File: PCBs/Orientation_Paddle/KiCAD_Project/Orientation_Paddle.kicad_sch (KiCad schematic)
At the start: 54 parts, among them J1 NP_Conn_01x04_Relief, J2 1-0001205, J3 NP_Conn_01x03_Relief, J4 NP_Conn_01x02_Relief, J5 NP_Conn_01x02_Relief, J6 NP_Conn_01x04, J7 NP_Conn_01x04, J8 NP_Conn_01x02, U1 1-0001232, U2 1-0001471, U3 1-0000207, Y1 1-0000721

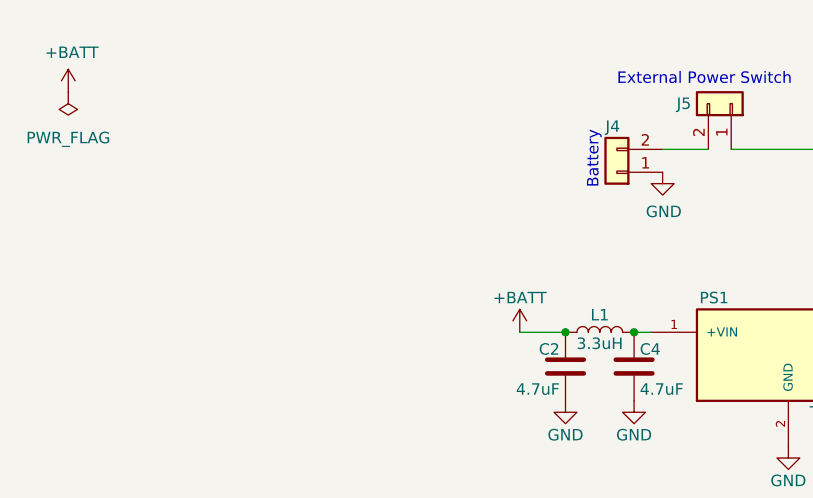
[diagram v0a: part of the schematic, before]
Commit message: Orientation Paddle Revisions: Board resize to nice numbers Fixed Footprint/Symbols causing ERC Errors Fixed remaining ERC Errors (Schematic and PCB)
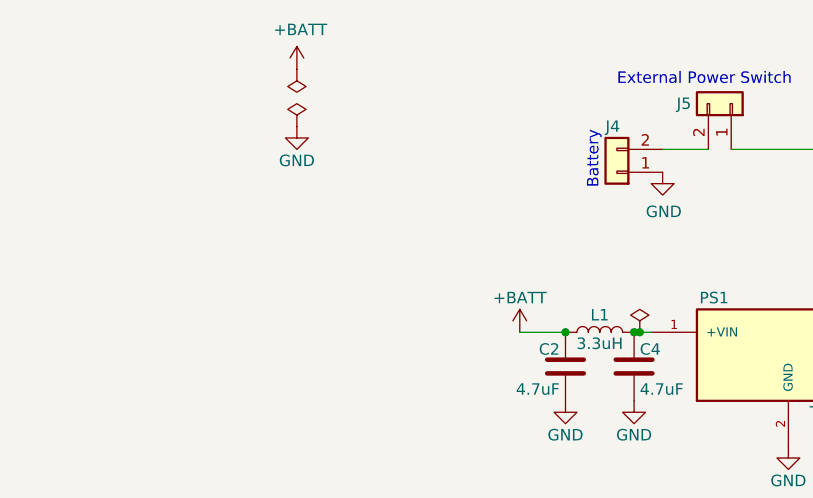
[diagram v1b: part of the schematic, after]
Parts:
- JP1, JP2, JP5, JP6: now left out of the parts list
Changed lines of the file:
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@@
 	)
 	(junction
+		(at 43.18 46.99)
+		(diameter 0)
+		(color 0 0 0 0)
+	)
+	(junction
 		(at 250.825 101.6)
 		(diameter 0)
@@
 	(wire
 		(pts
+			(xy 43.18 46.99) (xy 44.45 46.99)
+		)
+		(stroke
+			(width 0)
+			(type default)
+		)
+	)
+	(wire
+		(pts
 			(xy 255.905 104.14) (xy 255.905 104.775)
 		)
@@
 	(wire
 		(pts
-			(xy 42.545 46.99) (xy 44.45 46.99)
+			(xy 42.545 46.99) (xy 43.18 46.99)
 		)
 		(stroke
@@
 		(at 208.28 124.46 270)
 		(unit 1)
-		(exclude_from_sim no)
-		(in_bom yes)
+		(exclude_from_sim yes)
+		(in_bom no)
 		(on_board yes)
 		(dnp no)
@@
 	(symbol
 		(lib_id "power:PWR_FLAG")
-		(at -20.32 20.32 180)
+		(at 5.08 17.78 180)
 		(unit 1)
 		(exclude_from_sim no)
@@
 		(fields_autoplaced yes)
 		(property "Reference" "#FLG03"
-			(at -20.32 22.225 0)
+			(at 5.08 19.685 0)
 			(effects
 				(font
@@
 		)
 		(property "Value" "PWR_FLAG"
-			(at -20.32 25.4 0)
+			(at 5.08 22.86 0)
 			(effects
 				(font
 					(size 1.27 1.27)
 				)
+				(hide yes)
 			)
 		)
 		(property "Footprint" ""
-			(at -20.32 20.32 0)
+			(at 5.08 17.78 0)
 			(effects
 				(font
@@
 		)
 		(property "Datasheet" "~"
-			(at -20.32 20.32 0)
+			(at 5.08 17.78 0)
 			(effects
 				(font
@@
 		)
 		(property "Description" "Special symbol for telling ERC where power comes from"
-			(at -20.32 20.32 0)
+			(at 5.08 17.78 0)
 			(effects
 				(font
@@
 	)
 	(symbol
+		(lib_id "power:GND")
+		(at 5.08 24.13 0)
+		(unit 1)
+		(exclude_from_sim no)
+		(in_bom yes)
+		(on_board yes)
+		(dnp no)
+		(property "Reference" "#PWR056"
+			(at 5.08 30.48 0)
+			(effects
+				(font
+					(size 1.27 1.27)
+				)
+				(hide yes)
+			)
+		)
+		(property "Value" "GND"
+			(at 5.08 27.94 0)
+			(effects
+				(font
+					(size 1.27 1.27)
+				)
+			)
+		)
+		(property "Footprint" ""
+			(at 5.08 24.13 0)
+			(effects
+				(font
+					(size 1.27 1.27)
+				)
+				(hide yes)
+			)
+		)
+		(property "Datasheet" ""
+			(at 5.08 24.13 0)
+			(effects
+				(font
+					(size 1.27 1.27)
+				)
+				(hide yes)
+			)
+		)
+		(property "Description" "Power symbol creates a global label with name \"GND\" , ground"
+			(at 5.08 24.13 0)
+			(effects
+				(font
+					(size 1.27 1.27)
+				)
+				(hide yes)
+			)
+		)
+		(pin "1"
+		)
+		(instances
+			(project "Orientation_Paddle"
+				(path "/6c14ab86-27f6-4df4-bc2f-a5f06a463ed0"
+					(reference "#PWR056")
+					(unit 1)
+				)
+			)
+		)
+	)
+	(symbol
 		(lib_id "np_connectors:NP_Conn_01x03_Relief")
 		(at 20.32 157.48 180)
@@
 	)
 	(symbol
+		(lib_id "power:PWR_FLAG")
+		(at 5.08 24.13 0)
+		(unit 1)
+		(exclude_from_sim no)
+		(in_bom yes)
+		(on_board yes)
+		(dnp no)
+		(fields_autoplaced yes)
+		(property "Reference" "#FLG04"
+			(at 5.08 22.225 0)
+			(effects
+				(font
+					(size 1.27 1.27)
+				)
+				(hide yes)
+			)
+		)
+		(property "Value" "PWR_FLAG"
+			(at 5.08 19.05 0)
+			(effects
+				(font
+					(size 1.27 1.27)
+				)
+				(hide yes)
+			)
+		)
+		(property "Footprint" ""
+			(at 5.08 24.13 0)
+			(effects
+				(font
+					(size 1.27 1.27)
+				)
+				(hide yes)
+			)
+		)
+		(property "Datasheet" "~"
+			(at 5.08 24.13 0)
+			(effects
+				(font
+					(size 1.27 1.27)
+				)
+				(hide yes)
+			)
+		)
+		(property "Description" "Special symbol for telling ERC where power comes from"
+			(at 5.08 24.13 0)
+			(effects
+				(font
+					(size 1.27 1.27)
+				)
+				(hide yes)
+			)
+		)
+		(pin "1"
+		)
+		(instances
+			(project "Orientation_Paddle"
+				(path "/6c14ab86-27f6-4df4-bc2f-a5f06a463ed0"
+					(reference "#FLG04")
+					(unit 1)
+				)
+			)
+		)
+	)
+	(symbol
 		(lib_id "capacitors_0603:1-0000007")
 		(at 245.11 74.93 0)
@@
 	(symbol
 		(lib_id "power:+BATT")
-		(at -20.32 20.32 0)
+		(at 5.08 17.78 0)
 		(unit 1)
 		(exclude_from_sim no)
@@
 		(dnp no)
 		(property "Reference" "#PWR055"
-			(at -20.32 24.13 0)
+			(at 5.08 21.59 0)
 			(effects
 				(font
@@
 		)
 		(property "Value" "+BATT"
-			(at -19.939 15.9258 0)
+			(at 5.461 13.3858 0)
 			(effects
 				(font
@@
 		)
 		(property "Footprint" ""
-			(at -20.32 20.32 0)
+			(at 5.08 17.78 0)
 			(effects
 				(font
@@
 		)
 		(property "Datasheet" ""
-			(at -20.32 20.32 0)
+			(at 5.08 17.78 0)
 			(effects
 				(font
@@
 		)
 		(property "Description" "Power symbol creates a global label with name \"+BATT\""
-			(at -20.32 20.32 0)
+			(at 5.08 17.78 0)
 			(effects
 				(font
@@
 		(mirror x)
 		(unit 1)
-		(exclude_from_sim no)
-		(in_bom yes)
+		(exclude_from_sim yes)
+		(in_bom no)
 		(on_board yes)
 		(dnp no)
@@
 			)
 		)
-		(property "Description" ""
+		(property "Description" "Linear Regulator Replacement DC DC Converter 1 Output 3.3V - - - 500mA 4.75V - 32V Input"
 			(at 59.69 49.53 0)
 			(effects
@@
 		(at 208.28 111.76 270)
 		(unit 1)
-		(exclude_from_sim no)
-		(in_bom yes)
+		(exclude_from_sim yes)
+		(in_bom no)
 		(on_board yes)
 		(dnp no)
@@
 	)
 	(symbol
+		(lib_id "power:PWR_FLAG")
+		(at 43.18 46.99 0)
+		(unit 1)
+		(exclude_from_sim no)
+		(in_bom yes)
+		(on_board yes)
+		(dnp no)
+		(fields_autoplaced yes)
+		(property "Reference" "#FLG02"
+			(at 43.18 45.085 0)
+			(effects
+				(font
+					(size 1.27 1.27)
+				)
+				(hide yes)
+			)
+		)
+		(property "Value" "PWR_FLAG"
+			(at 43.18 42.7365 0)
+			(effects
+				(font
+					(size 1.27 1.27)
+				)
+				(hide yes)
+			)
+		)
+		(property "Footprint" ""
+			(at 43.18 46.99 0)
+			(effects
+				(font
+					(size 1.27 1.27)
+				)
+				(hide yes)
+			)
+		)
+		(property "Datasheet" "~"
+			(at 43.18 46.99 0)
+			(effects
+				(font
+					(size 1.27 1.27)
+				)
+				(hide yes)
+			)
+		)
+		(property "Description" "Special symbol for telling ERC where power comes from"
+			(at 43.18 46.99 0)
+			(effects
+				(font
+					(size 1.27 1.27)
+				)
+				(hide yes)
+			)
+		)
+		(pin "1"
+		)
+		(instances
+			(project "Orientation_Paddle"
+				(path "/6c14ab86-27f6-4df4-bc2f-a5f06a463ed0"
+					(reference "#FLG02")
+					(unit 1)
+				)
+			)
+		)
+	)
+	(symbol
 		(lib_id "capacitors_0603:1-0000007")
 		(at 29.21 152.4 90)
@@
 		(mirror x)
 		(unit 1)
-		(exclude_from_sim no)
-		(in_bom yes)
+		(exclude_from_sim yes)
+		(in_bom no)
 		(on_board yes)
 		(dnp no)

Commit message: Fixed Orientation Paddle ERC Issues and Copper to Edge Clearence
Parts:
- H1, H2, H3, H4: now left out of the parts list
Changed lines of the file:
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@@
 		(unit 1)
 		(exclude_from_sim no)
-		(in_bom yes)
+		(in_bom no)
 		(on_board yes)
 		(dnp no)
@@
 		(unit 1)
 		(exclude_from_sim no)
-		(in_bom yes)
+		(in_bom no)
 		(on_board yes)
 		(dnp no)
@@
 		(unit 1)
 		(exclude_from_sim no)
-		(in_bom yes)
+		(in_bom no)
 		(on_board yes)
 		(dnp no)
@@
 		(unit 1)
 		(exclude_from_sim no)
-		(in_bom yes)
+		(in_bom no)
 		(on_board yes)
 		(dnp no)
